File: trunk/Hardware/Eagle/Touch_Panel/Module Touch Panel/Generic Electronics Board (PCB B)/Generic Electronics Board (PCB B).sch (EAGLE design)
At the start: 41 parts, among them IC1 ST3485, U1 XMEGA-A4TQFP, U2 SPX1117M3-L-3-3, X1 RJ45-8L-B, X6 RJ45-8L-B

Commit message: Work in progress
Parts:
- added D1: (no value), diode:DIODE-DO-214AC
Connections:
- net +12V: now also D1.C
- net BUS_PWR: now also D1.A
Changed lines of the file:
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@@
 <part name="+3V16" library="supply1" deviceset="+3V3" device=""/>
 <part name="GND26" library="supply1" deviceset="GND" device=""/>
-<part name="P+2" library="supply1" deviceset="VCC" device="" value="+12V"/>
+<part name="D1" library="diode" deviceset="DIODE-" device="DO-214AC"/>
+<part name="BUS_PWR1" library="supply1" deviceset="VCC" device="" value="BUS_PWR"/>
 </parts>
 <sheets>
@@
 <instance part="+3V16" gate="G$1" x="416.56" y="38.1"/>
 <instance part="GND26" gate="1" x="416.56" y="20.32"/>
-<instance part="P+2" gate="VCC" x="365.76" y="83.82"/>
+<instance part="D1" gate="G$1" x="360.68" y="78.74"/>
+<instance part="BUS_PWR1" gate="VCC" x="355.6" y="83.82"/>
 </instances>
 <busses>
@@
 <junction x="325.12" y="55.88"/>
 </segment>
+<segment>
+<pinref part="BUS_PWR1" gate="VCC" pin="VCC"/>
+<pinref part="D1" gate="G$1" pin="A"/>
+<wire x1="355.6" y1="81.28" x2="355.6" y2="78.74" width="0.1524" layer="91"/>
+<wire x1="355.6" y1="78.74" x2="358.14" y2="78.74" width="0.1524" layer="91"/>
+</segment>
 </net>
 <net name="N$16" class="0">
@@
 <junction x="375.92" y="78.74"/>
 <pinref part="U2" gate="G$1" pin="VIN"/>
-<pinref part="P+2" gate="VCC" pin="VCC"/>
-<wire x1="365.76" y1="81.28" x2="365.76" y2="78.74" width="0.1524" layer="91"/>
 <pinref part="C5" gate="G$1" pin="+"/>
 <wire x1="365.76" y1="73.66" x2="365.76" y2="78.74" width="0.1524" layer="91"/>
+<pinref part="D1" gate="G$1" pin="C"/>
+<wire x1="363.22" y1="78.74" x2="365.76" y2="78.74" width="0.1524" layer="91"/>
 <junction x="365.76" y="78.74"/>
 </segment>

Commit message: Touch Panel PCB_A & PCB_B final version (to electrical&part check)
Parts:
- removed C8, C9: 22n, rcl:C-EUC1206
- removed R48: 330R, rcl:R-EU_M0805
- added JP6: (no value), pinhead:PINHD-2X3SMD
- added R15, R16, R17, R18: 470k, rcl:R-EU_R0603
- added R19, R20, R21, R22, R3, R4: 1k, rcl:R-EU_R0603
- C1, C2, C4, C7: value 22n -> 4n7; device rcl:C-EUC1206 -> rcl:C-EUC0603
- C10, C12, C15, C16, C17, C6: device rcl:C-EUC1206 -> rcl:C-EUC0603
- C3: device rcl:C-EUC0805 -> rcl:C-EUC0603
- JP2, JP3, JP4, JP5: device pinhead:PINHD-2X2SMD -> pinhead:PINHD-2X2
- R1, R11, R12, R14, R2, R8: value 10k -> 1k; device rcl:R-EU_R1206 -> rcl:R-EU_R0603
- R10, R13, R5, R6, R7, R9: device rcl:R-EU_M0805 -> rcl:R-EU_R0603
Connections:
- removed net JP1: R11.2
- removed net JP2: R12.2
- removed net JP3: R14.2
- removed net JP4: R2.2
- removed net JP5: R1.2
- removed net JP6: R8.2
- removed net N$16: IC1.!RE, R48.2
- removed net N$26: C8.1, R12.1, U1.PC5(OC1B/MOSI/XCK1)
- removed net N$27: C1.2, U1.PA2(ADC2)
- removed net N$28: C7.1, R11.1, U1.PC3(OC0D/TXD0)
- removed net N$29: C4.2, U1.PA4(ADC4)
- new net CLK/SCK: JP6.6, U1.PD7(TXD1/SCK/CLKO/EVO)
- new net LA/: JP6.5, U1.PD6(RXD1/MISO)
- new net N$10: R8.1, U1.PC4(OC1A/!SS!)
- new net N$11: R11.1, U1.PC5(OC1B/MOSI/XCK1)
- new net N$12: R12.1, U1.PC6(MISO/RXD1)
- new net N$19: C1.2, R20.1, U1.PB1(ADC9)
- new net N$22: C4.2, R22.1, U1.PB3(ADC11/DAC1)
- new net N$23: C7.1, R16.2, U1.PA4(ADC4)
- new net N$24: C4.1, R15.2, U1.PA3(ADC3)
- new net N$25: R15.1, R16.1, R17.1, R18.1, U1.PA2(ADC2)
- new net N$9: R4.1, U1.PC3(OC0D/TXD0)
- new net OPTO: JP3.1, U1.PA1(ADC1)
- new net SDI/MOSI: JP6.4, U1.PD5(OC1B/XCK1/MOSI)
- new net X5: JP5.4, R11.2
- new net X6: JP5.3, R12.2
- new net X7: JP5.1, R14.2
- new net Y3: JP3.4, R19.2
- net +3V3: now also JP6.2
- net GND: now also JP6.1, U1.PA7/(ADC7/AC0-OUT); no longer JP3.1, R48.1
- net N$1: now also R1.1, U1.PC0(OC0A/SDA); no longer C2.2, U1.PA0(ADC0/AREF)
- net N$13: now also R14.1, U1.PC7(SCK/TXD1/CLKO/EVO); no longer C2.1, R1.1, U1.PA1(ADC1)
- net N$17: now also C2.1, R18.2, U1.PA6(ADC6); no longer C8.2, U1.PC4(OC1A/!SS!)
- net N$18: now also C2.2, R19.1, U1.PB0(ADC8/AREF); no longer C4.1, R2.1, U1.PA5(ADC5)
- net N$2: now also R2.1, U1.PC1(OC0B/XCK0/SCL); no longer C1.1, R8.1, U1.PA3(ADC3)
- net N$20: now also C1.1, R17.2, U1.PA5(ADC5); no longer C7.2, U1.PC2(OC0C/RXD0)
- net N$21: now also C7.2, R21.1, U1.PB2(ADC10/DAC0); no longer C9.1, R14.1, U1.PC7(SCK/TXD1/CLKO/EVO)
- net N$3: now also R3.1, U1.PC2(OC0C/RXD0); no longer C9.2, U1.PC6(MISO/RXD1)
- net N$6: now also IC1.!RE
- net X0: now also R1.2
- net X1: now also R2.2
- net X2: now also R3.2
- net X3: now also JP4.1, R4.2; no longer JP5.2
- net X4: now also JP5.2, R8.2; no longer JP5.4
- net Y0: now also R22.2
- net Y1: now also R21.2
- net Y2: now also R20.2
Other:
- moved on the sheet: C1, C2, C4, C7, R1, R11, R12, R14, R2, R8

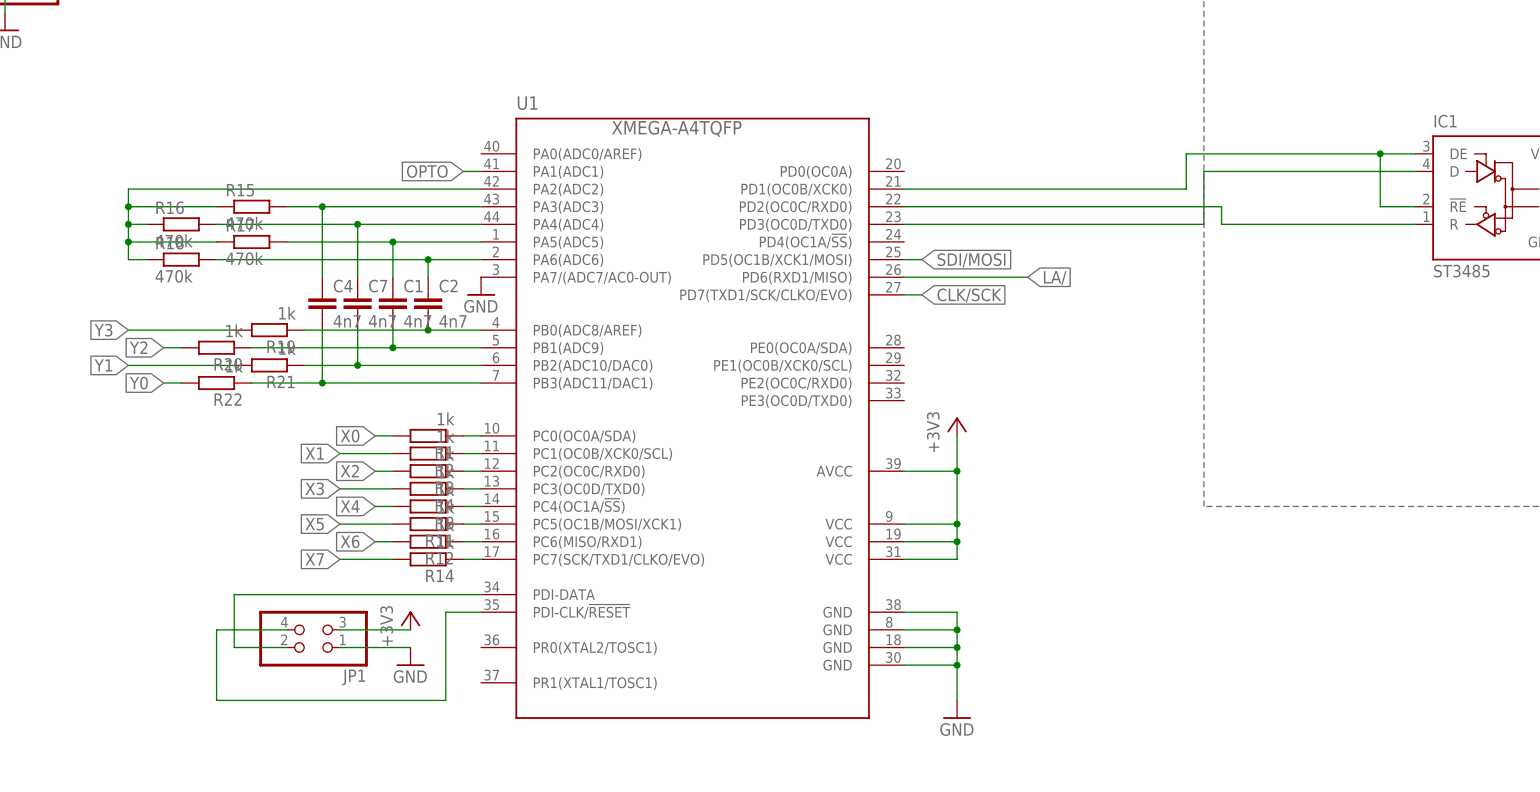
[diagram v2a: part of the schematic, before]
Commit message: 
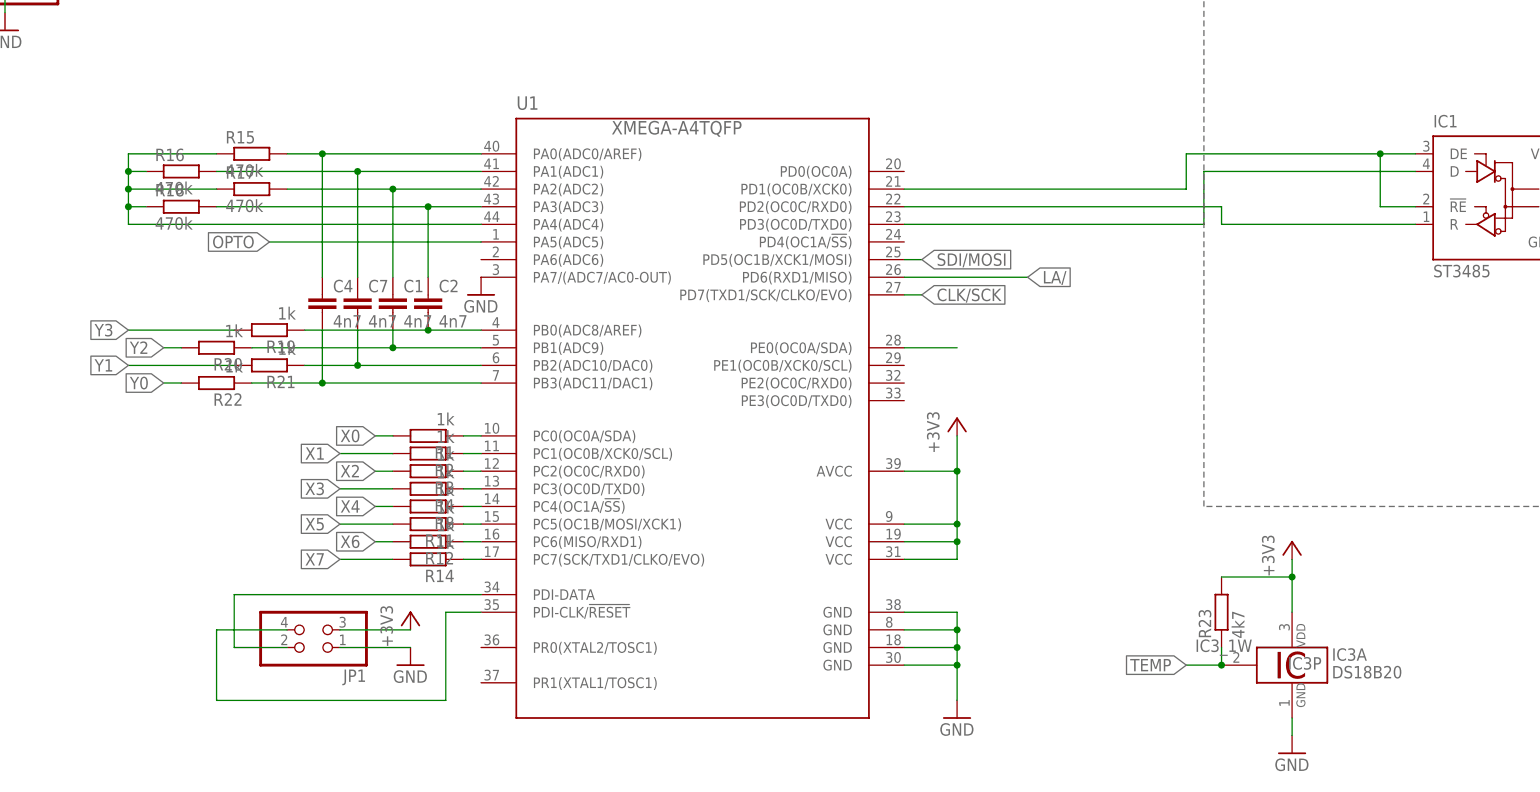
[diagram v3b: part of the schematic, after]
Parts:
- added IC3: DS18B20, 1wire:DS18B20
- added R23: 4k7, rcl:R-EU_R0603
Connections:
- new net TEMP: IC3_1W.1W, R23.1, U1.PE0(OC0A/SDA)
- net +3V3: now also IC3P.VDD, R23.2
- net GND: now also IC3P.GND
- net N$17: now also U1.PA3(ADC3); no longer U1.PA6(ADC6)
- net N$20: now also U1.PA2(ADC2); no longer U1.PA5(ADC5)
- net N$23: now also U1.PA1(ADC1); no longer U1.PA4(ADC4)
- net N$24: now also U1.PA0(ADC0/AREF); no longer U1.PA3(ADC3)
- net N$25: now also U1.PA4(ADC4); no longer U1.PA2(ADC2)
- net OPTO: now also U1.PA5(ADC5); no longer U1.PA1(ADC1)
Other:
- moved on the sheet: R15, R16, R17, R18
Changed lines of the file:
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@@
 <part name="GND7" library="supply1" deviceset="GND" device=""/>
 <part name="+3V4" library="supply1" deviceset="+3V3" device=""/>
+<part name="IC3" library="1wire" deviceset="DS18B20" device=""/>
+<part name="GND4" library="supply1" deviceset="GND" device=""/>
+<part name="+3V9" library="supply1" deviceset="+3V3" device=""/>
+<part name="R23" library="rcl" deviceset="R-EU_" device="R0603" value="4k7"/>
 </parts>
 <sheets>
@@
 <instance part="C7" gate="G$1" x="50.8" y="7.62"/>
 <instance part="GND1" gate="1" x="68.58" y="7.62"/>
-<instance part="R15" gate="G$1" x="35.56" y="20.32"/>
-<instance part="R16" gate="G$1" x="25.4" y="17.78"/>
-<instance part="R17" gate="G$1" x="35.56" y="15.24"/>
-<instance part="R18" gate="G$1" x="25.4" y="12.7"/>
+<instance part="R15" gate="G$1" x="35.56" y="27.94"/>
+<instance part="R16" gate="G$1" x="25.4" y="25.4"/>
+<instance part="R17" gate="G$1" x="35.56" y="22.86"/>
+<instance part="R18" gate="G$1" x="25.4" y="20.32"/>
 <instance part="R19" gate="G$1" x="38.1" y="2.54" rot="R180"/>
 <instance part="R20" gate="G$1" x="30.48" y="0" rot="R180"/>
@@
 <instance part="GND7" gate="1" x="0" y="45.72"/>
 <instance part="+3V4" gate="G$1" x="0" y="71.12"/>
+<instance part="IC3" gate="_1W" x="180.34" y="-45.72"/>
+<instance part="IC3" gate="A" x="185.42" y="-45.72"/>
+<instance part="IC3" gate="P" x="185.42" y="-45.72"/>
+<instance part="GND4" gate="1" x="185.42" y="-58.42"/>
+<instance part="+3V9" gate="G$1" x="185.42" y="-27.94"/>
+<instance part="R23" gate="G$1" x="175.26" y="-38.1" rot="R90"/>
 </instances>
 <busses>
@@
 <wire x1="0" y1="48.26" x2="0" y2="53.34" width="0.1524" layer="91"/>
 </segment>
+<segment>
+<pinref part="IC3" gate="P" pin="GND"/>
+<pinref part="GND4" gate="1" pin="GND"/>
+<wire x1="185.42" y1="-53.34" x2="185.42" y2="-55.88" width="0.1524" layer="91"/>
+</segment>
 </net>
 <net name="+3V3" class="0">
@@
 <wire x1="0" y1="60.96" x2="0" y2="68.58" width="0.1524" layer="91"/>
 </segment>
+<segment>
+<pinref part="IC3" gate="P" pin="VDD"/>
+<pinref part="+3V9" gate="G$1" pin="+3V3"/>
+<wire x1="185.42" y1="-38.1" x2="185.42" y2="-33.02" width="0.1524" layer="91"/>
+<pinref part="R23" gate="G$1" pin="2"/>
+<wire x1="185.42" y1="-33.02" x2="185.42" y2="-30.48" width="0.1524" layer="91"/>
+<wire x1="175.26" y1="-33.02" x2="185.42" y2="-33.02" width="0.1524" layer="91"/>
+<junction x="185.42" y="-33.02"/>
+</segment>
 </net>
 <net name="Y0" class="0">
@@
 </segment>
 <segment>
-<pinref part="U1" gate="G$1" pin="PA1(ADC1)"/>
-<wire x1="68.58" y1="25.4" x2="66.04" y2="25.4" width="0.1524" layer="91"/>
-<label x="66.04" y="25.4" size="1.778" layer="95" rot="R180" xref="yes"/>
+<pinref part="U1" gate="G$1" pin="PA5(ADC5)"/>
+<wire x1="68.58" y1="15.24" x2="38.1" y2="15.24" width="0.1524" layer="91"/>
+<label x="38.1" y="15.24" size="1.778" layer="95" rot="R180" xref="yes"/>
 </segment>
 </net>
@@
 <segment>
 <pinref part="C2" gate="G$1" pin="1"/>
-<pinref part="U1" gate="G$1" pin="PA6(ADC6)"/>
-<wire x1="60.96" y1="10.16" x2="60.96" y2="12.7" width="0.1524" layer="91"/>
-<wire x1="60.96" y1="12.7" x2="68.58" y2="12.7" width="0.1524" layer="91"/>
+<wire x1="60.96" y1="10.16" x2="60.96" y2="20.32" width="0.1524" layer="91"/>
 <pinref part="R18" gate="G$1" pin="2"/>
-<wire x1="30.48" y1="12.7" x2="60.96" y2="12.7" width="0.1524" layer="91"/>
-<junction x="60.96" y="12.7"/>
+<wire x1="30.48" y1="20.32" x2="60.96" y2="20.32" width="0.1524" layer="91"/>
+<pinref part="U1" gate="G$1" pin="PA3(ADC3)"/>
+<wire x1="68.58" y1="20.32" x2="60.96" y2="20.32" width="0.1524" layer="91"/>
+<junction x="60.96" y="20.32"/>
 </segment>
 </net>
@@
 <segment>
 <pinref part="C1" gate="G$1" pin="1"/>
-<pinref part="U1" gate="G$1" pin="PA5(ADC5)"/>
-<wire x1="55.88" y1="10.16" x2="55.88" y2="15.24" width="0.1524" layer="91"/>
-<wire x1="55.88" y1="15.24" x2="68.58" y2="15.24" width="0.1524" layer="91"/>
+<wire x1="55.88" y1="10.16" x2="55.88" y2="22.86" width="0.1524" layer="91"/>
 <pinref part="R17" gate="G$1" pin="2"/>
-<wire x1="40.64" y1="15.24" x2="55.88" y2="15.24" width="0.1524" layer="91"/>
-<junction x="55.88" y="15.24"/>
+<wire x1="40.64" y1="22.86" x2="55.88" y2="22.86" width="0.1524" layer="91"/>
+<pinref part="U1" gate="G$1" pin="PA2(ADC2)"/>
+<wire x1="68.58" y1="22.86" x2="55.88" y2="22.86" width="0.1524" layer="91"/>
+<junction x="55.88" y="22.86"/>
 </segment>
 </net>
@@
 <segment>
 <pinref part="C7" gate="G$1" pin="1"/>
+<wire x1="50.8" y1="10.16" x2="50.8" y2="25.4" width="0.1524" layer="91"/>
+<pinref part="R16" gate="G$1" pin="2"/>
+<wire x1="30.48" y1="25.4" x2="50.8" y2="25.4" width="0.1524" layer="91"/>
+<pinref part="U1" gate="G$1" pin="PA1(ADC1)"/>
+<wire x1="68.58" y1="25.4" x2="50.8" y2="25.4" width="0.1524" layer="91"/>
+<junction x="50.8" y="25.4"/>
+</segment>
+</net>
+<net name="N$24" class="0">
+<segment>
+<pinref part="C4" gate="G$1" pin="1"/>
+<wire x1="45.72" y1="10.16" x2="45.72" y2="27.94" width="0.1524" layer="91"/>
+<pinref part="R15" gate="G$1" pin="2"/>
+<wire x1="40.64" y1="27.94" x2="45.72" y2="27.94" width="0.1524" layer="91"/>
+<pinref part="U1" gate="G$1" pin="PA0(ADC0/AREF)"/>
+<wire x1="68.58" y1="27.94" x2="45.72" y2="27.94" width="0.1524" layer="91"/>
+<junction x="45.72" y="27.94"/>
+</segment>
+</net>
+<net name="N$25" class="0">
+<segment>
+<pinref part="R18" gate="G$1" pin="1"/>
+<wire x1="20.32" y1="20.32" x2="17.78" y2="20.32" width="0.1524" layer="91"/>
+<wire x1="17.78" y1="20.32" x2="17.78" y2="22.86" width="0.1524" layer="91"/>
+<wire x1="17.78" y1="22.86" x2="17.78" y2="25.4" width="0.1524" layer="91"/>
+<wire x1="17.78" y1="25.4" x2="17.78" y2="27.94" width="0.1524" layer="91"/>
+<pinref part="R17" gate="G$1" pin="1"/>
+<wire x1="30.48" y1="22.86" x2="17.78" y2="22.86" width="0.1524" layer="91"/>
+<pinref part="R16" gate="G$1" pin="1"/>
+<wire x1="20.32" y1="25.4" x2="17.78" y2="25.4" width="0.1524" layer="91"/>
+<pinref part="R15" gate="G$1" pin="1"/>
+<wire x1="30.48" y1="27.94" x2="17.78" y2="27.94" width="0.1524" layer="91"/>
+<junction x="17.78" y="25.4"/>
+<junction x="17.78" y="22.86"/>
 <pinref part="U1" gate="G$1" pin="PA4(ADC4)"/>
-<wire x1="50.8" y1="10.16" x2="50.8" y2="17.78" width="0.1524" layer="91"/>
-<wire x1="50.8" y1="17.78" x2="68.58" y2="17.78" width="0.1524" layer="91"/>
-<pinref part="R16" gate="G$1" pin="2"/>
-<wire x1="30.48" y1="17.78" x2="50.8" y2="17.78" width="0.1524" layer="91"/>
-<junction x="50.8" y="17.78"/>
-</segment>
-</net>
-<net name="N$24" class="0">
-<segment>
-<pinref part="C4" gate="G$1" pin="1"/>
-<pinref part="U1" gate="G$1" pin="PA3(ADC3)"/>
-<wire x1="45.72" y1="10.16" x2="45.72" y2="20.32" width="0.1524" layer="91"/>
-<wire x1="45.72" y1="20.32" x2="68.58" y2="20.32" width="0.1524" layer="91"/>
-<pinref part="R15" gate="G$1" pin="2"/>
-<wire x1="40.64" y1="20.32" x2="45.72" y2="20.32" width="0.1524" layer="91"/>
-<junction x="45.72" y="20.32"/>
-</segment>
-</net>
-<net name="N$25" class="0">
-<segment>
-<pinref part="R18" gate="G$1" pin="1"/>
-<wire x1="20.32" y1="12.7" x2="17.78" y2="12.7" width="0.1524" layer="91"/>
-<pinref part="U1" gate="G$1" pin="PA2(ADC2)"/>
-<wire x1="17.78" y1="12.7" x2="17.78" y2="15.24" width="0.1524" layer="91"/>
-<wire x1="17.78" y1="15.24" x2="17.78" y2="17.78" width="0.1524" layer="91"/>
+<wire x1="68.58" y1="17.78" x2="17.78" y2="17.78" width="0.1524" layer="91"/>
 <wire x1="17.78" y1="17.78" x2="17.78" y2="20.32" width="0.1524" layer="91"/>
-<wire x1="17.78" y1="20.32" x2="17.78" y2="22.86" width="0.1524" layer="91"/>
-<wire x1="17.78" y1="22.86" x2="68.58" y2="22.86" width="0.1524" layer="91"/>
-<pinref part="R17" gate="G$1" pin="1"/>
-<wire x1="30.48" y1="15.24" x2="17.78" y2="15.24" width="0.1524" layer="91"/>
-<pinref part="R16" gate="G$1" pin="1"/>
-<wire x1="20.32" y1="17.78" x2="17.78" y2="17.78" width="0.1524" layer="91"/>
-<pinref part="R15" gate="G$1" pin="1"/>
-<wire x1="30.48" y1="20.32" x2="17.78" y2="20.32" width="0.1524" layer="91"/>
 <junction x="17.78" y="20.32"/>
-<junction x="17.78" y="17.78"/>
-<junction x="17.78" y="15.24"/>
 </segment>
 </net>
@@
 </segment>
 </net>
+<net name="TEMP" class="0">
+<segment>
+<pinref part="IC3" gate="_1W" pin="1W"/>
+<wire x1="175.26" y1="-45.72" x2="170.18" y2="-45.72" width="0.1524" layer="91"/>
+<label x="170.18" y="-45.72" size="1.778" layer="95" rot="R180" xref="yes"/>
+<pinref part="R23" gate="G$1" pin="1"/>
+<wire x1="175.26" y1="-43.18" x2="175.26" y2="-45.72" width="0.1524" layer="91"/>
+<junction x="175.26" y="-45.72"/>
+</segment>
+<segment>
+<pinref part="U1" gate="G$1" pin="PE0(OC0A/SDA)"/>
+<wire x1="129.54" y1="0" x2="137.16" y2="0" width="0.1524" layer="91"/>
+</segment>
+</net>

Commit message: Touch Panel (PCBA+PCBB) ver. 1.00
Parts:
- added R24: 11k, rcl:R-EU_R0603
- added R25: 100k, rcl:R-EU_R0603
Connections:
- new net POWER_METER: R24.2, R25.1, U1.PA6(ADC6)
- net BUS_PWR: now also R25.2
- net GND: now also R24.1
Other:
- note added: "PCB (A-B) CONNECTORS"
- moved on the sheet: JP2, JP3, JP4, JP5, JP6

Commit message: Minor changes
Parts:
- C4: value 4n7 -> 4n7 (22n)
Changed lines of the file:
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@@
 <part name="R14" library="rcl" deviceset="R-EU_" device="R0603" value="1k"/>
 <part name="C1" library="rcl" deviceset="C-EU" device="C0603" value="4n7"/>
-<part name="C4" library="rcl" deviceset="C-EU" device="C0603" value="4n7"/>
+<part name="C4" library="rcl" deviceset="C-EU" device="C0603" value="4n7 (22n)"/>
 <part name="C7" library="rcl" deviceset="C-EU" device="C0603" value="4n7"/>
 <part name="GND1" library="supply1" deviceset="GND" device=""/>

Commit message: PDI signals renamed.
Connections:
- net N$3 renamed PC2
- net N$7 renamed PDI_DATA
- net N$8 renamed PDI_CLK
- net N$9 renamed PC3
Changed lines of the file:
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@@
 <?xml version="1.0" encoding="utf-8"?>
 <!DOCTYPE eagle SYSTEM "eagle.dtd">
-<eagle version="6.1">
+<eagle version="6.4">
 <drawing>
 <settings>
@@
 </segment>
 </net>
-<net name="N$7" class="0">
+<net name="PDI_DATA" class="0">
 <segment>
 <pinref part="U1" gate="G$1" pin="PDI-DATA"/>
@@
 </segment>
 </net>
-<net name="N$8" class="0">
+<net name="PDI_CLK" class="0">
 <segment>
 <pinref part="U1" gate="G$1" pin="PDI-CLK/!RESET"/>
@@
 </segment>
 </net>
-<net name="N$3" class="0">
+<net name="PC2" class="0">
 <segment>
 <pinref part="R3" gate="G$1" pin="1"/>
@@
 </segment>
 </net>
-<net name="N$9" class="0">
+<net name="PC3" class="0">
 <segment>
 <pinref part="R4" gate="G$1" pin="1"/>
